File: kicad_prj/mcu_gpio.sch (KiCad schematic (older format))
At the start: 1 part

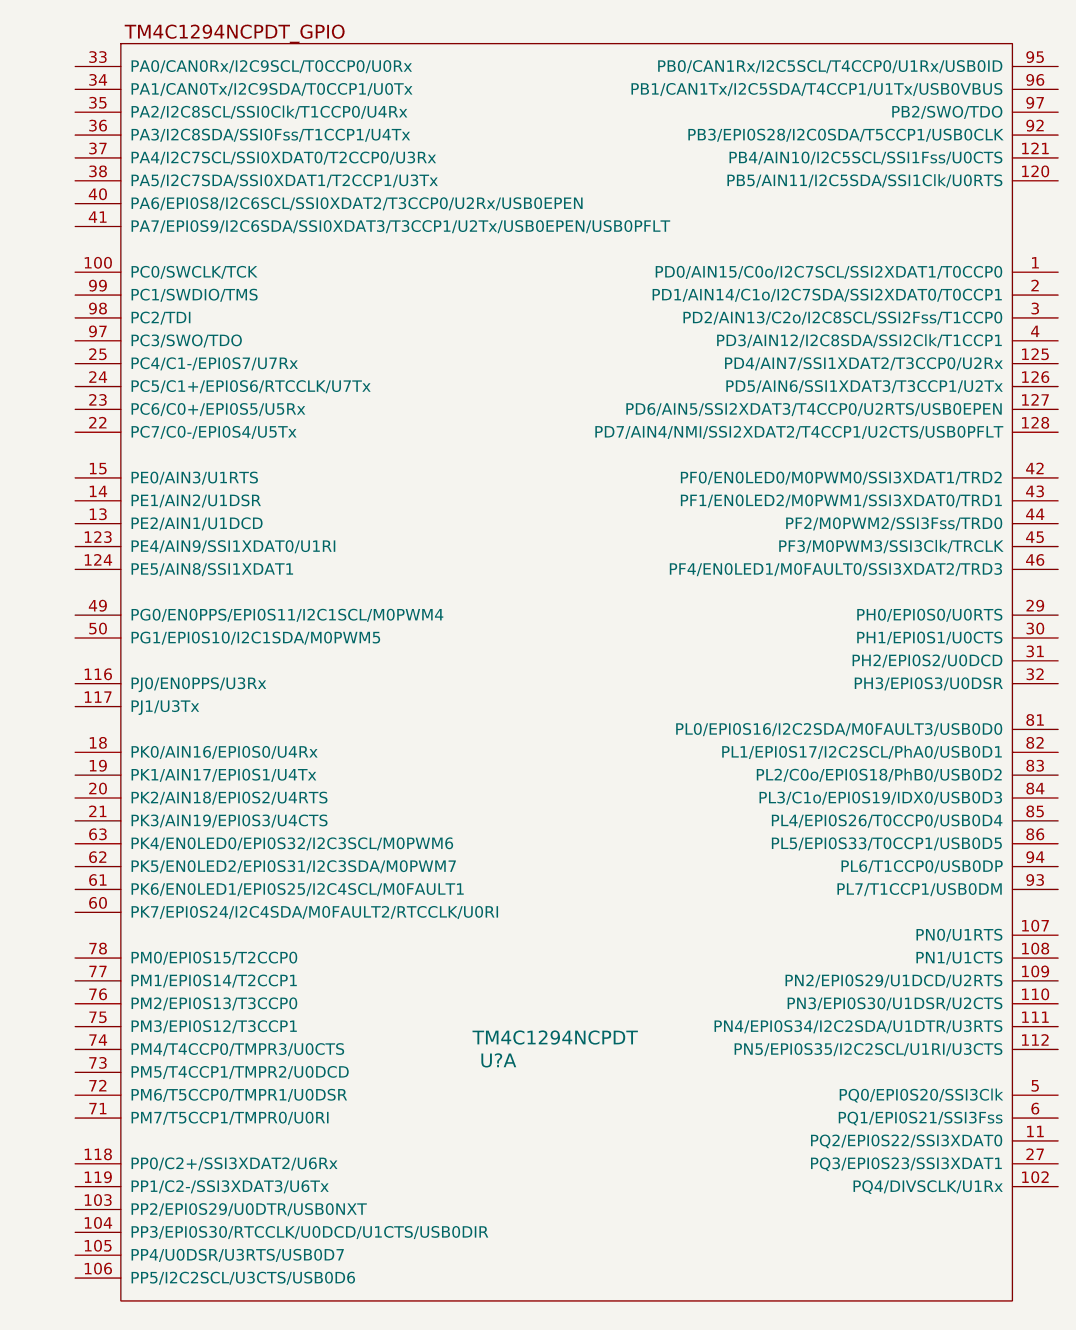
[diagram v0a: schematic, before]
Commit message: Corrected sheet sizes
A4 to A size on all sheets
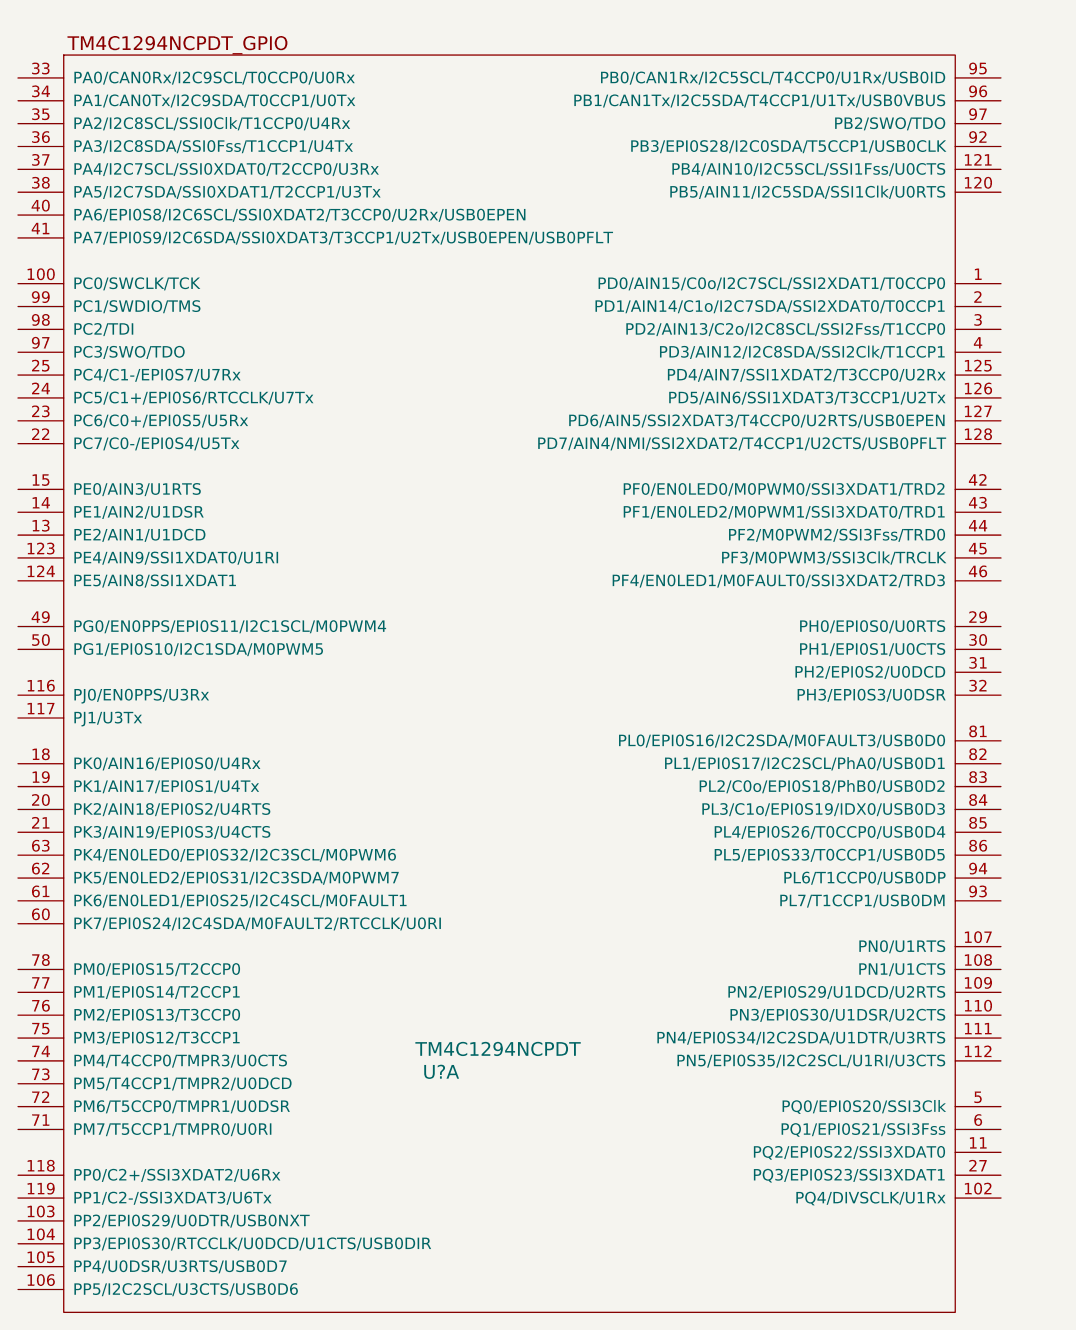
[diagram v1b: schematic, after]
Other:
- moved on the sheet: U?A
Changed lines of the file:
@@
 EELAYER 25 0
 EELAYER END
-$Descr A4 11693 8268
+$Descr A 11000 8500
 encoding utf-8
 Sheet 12 13
@@
 L TM4C1294NCPDT U?
 U 1 1 566CD626
-P 5700 3600
-F 0 "U?" H 5450 1950 60  0000 C CNN
-F 1 "TM4C1294NCPDT" H 5700 2050 60  0000 C CNN
-F 2 "" H 4100 5950 60  0000 C CNN
-F 3 "" H 4100 5950 60  0000 C CNN
-	1    5700 3600
+P 5450 3650
+F 0 "U?" H 5200 2000 60  0000 C CNN
+F 1 "TM4C1294NCPDT" H 5450 2100 60  0000 C CNN
+F 2 "" H 3850 6000 60  0000 C CNN
+F 3 "" H 3850 6000 60  0000 C CNN
+	1    5450 3650
 	1    0    0    -1
 $EndComp
